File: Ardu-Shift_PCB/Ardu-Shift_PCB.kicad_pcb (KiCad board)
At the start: 2 copper layers, 103.5 x 62.2 mm, 16 parts, among them U1 OLED(SPI), U2 Arduino_Pro_Micro

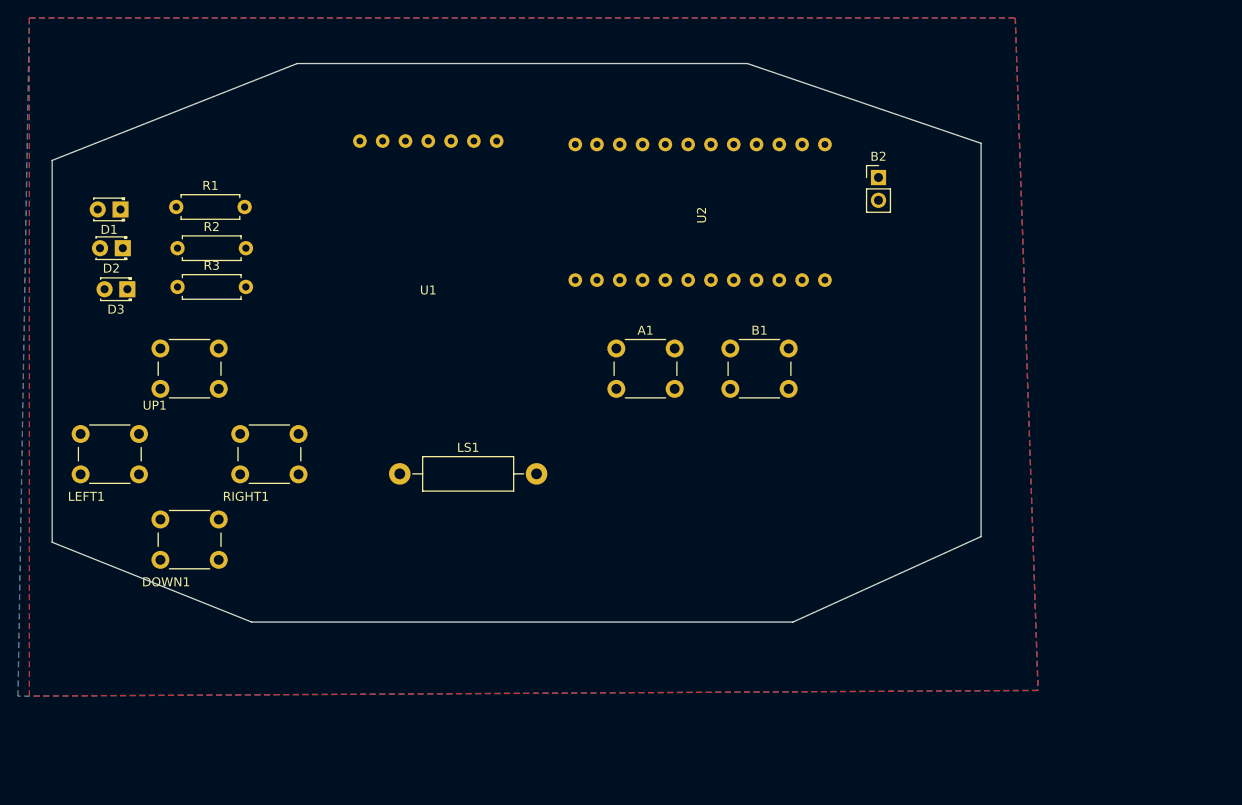
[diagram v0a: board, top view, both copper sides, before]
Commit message: more 'realistic' adjustments to the location of electronics on the PCB
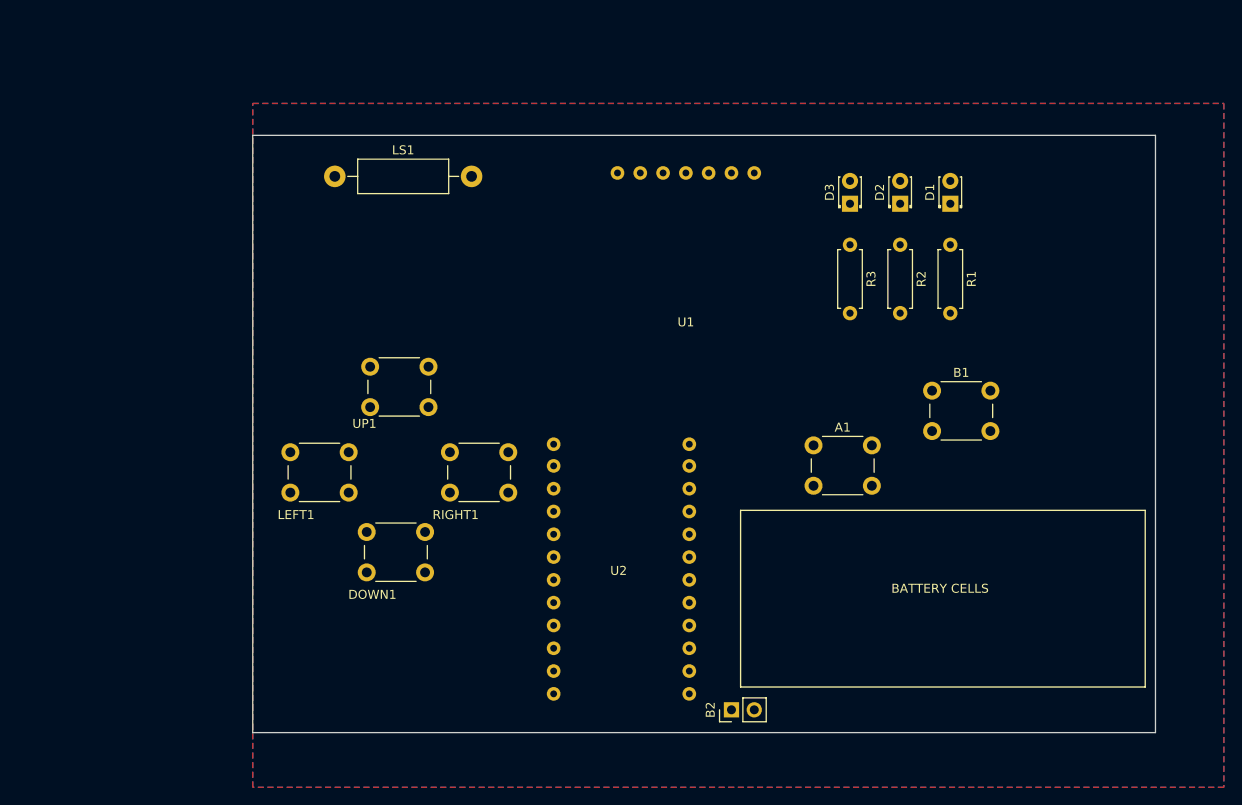
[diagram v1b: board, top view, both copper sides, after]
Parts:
- moved D1 92.5 mm to (115.3, 41.7), turned to 90 degrees
- moved D2 86.8 mm to (109.7, 41.7), turned to 90 degrees
- moved R1 86.4 mm to (115.3, 46.2), turned to 270 degrees
- moved D3 81.1 mm to (104.1, 41.7), turned to 90 degrees
- moved R2 80.5 mm to (109.7, 46.2), turned to 270 degrees
- moved R3 75.1 mm to (104.1, 46.2), turned to 270 degrees
- moved B2 61.5 mm to (90.9, 98.0), turned to 90 degrees
- moved U2 45.6 mm to (78.7, 86.4), turned to 180 degrees
- moved LS1 33.9 mm to (46.7, 38.6)
- moved U1 28.9 mm to (85.9, 54.4)
- moved A1 24.5 mm to (100.1, 68.6)
- moved LEFT1 23.5 mm to (41.8, 69.3)
- moved RIGHT1 23.5 mm to (59.6, 69.3)
- moved UP1 23.5 mm to (50.7, 59.8)
- moved DOWN1 23.0 mm to (50.3, 78.2)
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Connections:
- DOWN1 pad 2: Net-(DOWN1-Pad2) -> BAT-
- LEFT1 pad 1: Net-(LEFT1-Pad1) -> LEFT
- LEFT1 pad 2: BAT- -> Net-(LEFT1-Pad2)
- RIGHT1 pad 2: BAT- -> Net-(RIGHT1-Pad2)
- U2 pad 2: UP -> B
- U2 pad 3: LEFT -> A
- U2 pad 4: RIGHT -> Speaker-
- U2 pad 5: DOWN -> Speaker+
- U2 pad A0: B -> UP
- U2 pad A1: A -> LEFT
- U2 pad A2: Speaker- -> RIGHT
- U2 pad A3: Speaker+ -> DOWN
- UP1 pad 1: UP -> Net-(UP1-Pad1)
- UP1 pad 2: BAT- -> Net-(UP1-Pad2)
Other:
- board size 103.5 x 62.2 mm -> 100.6 x 66.5 mm

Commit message: first version of the final assembly/routing of game-device PCB
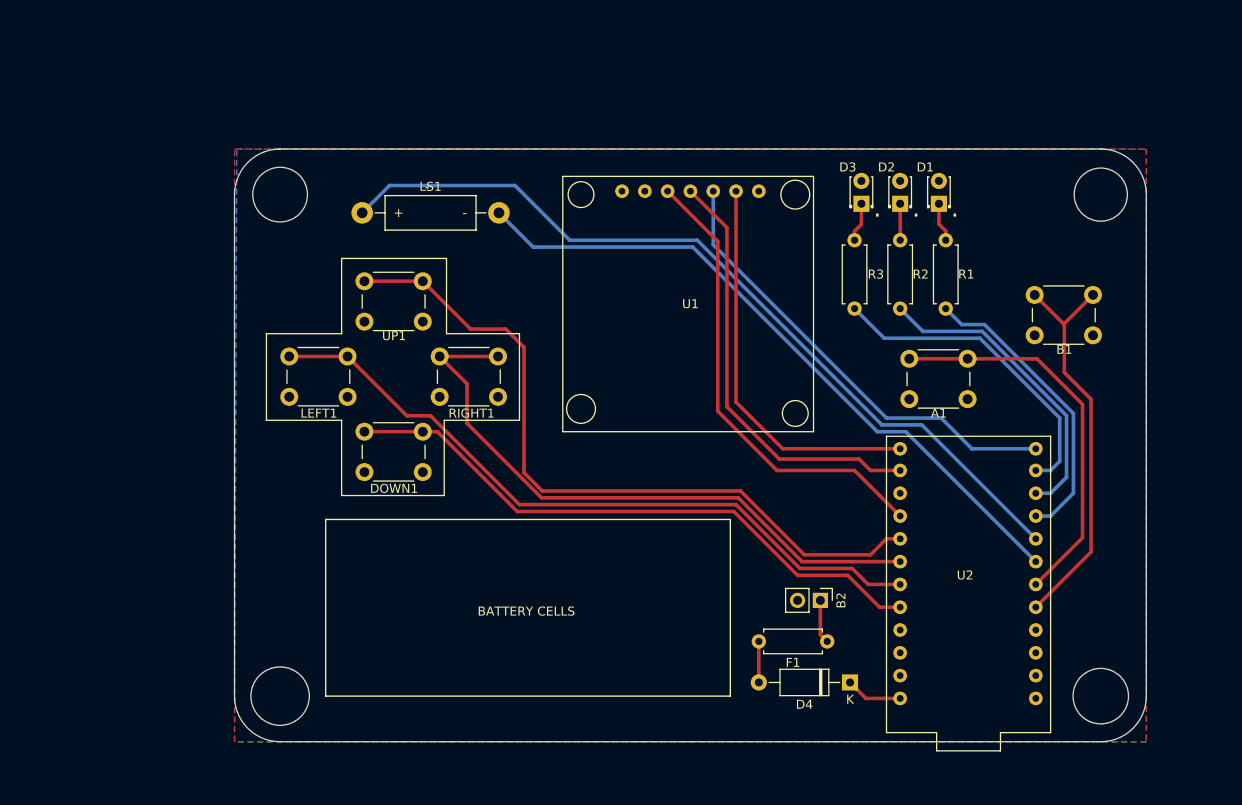
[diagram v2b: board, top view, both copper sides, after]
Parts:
- added D4: D, Diode_THT:D_A-405_P10.16mm_Horizontal, F.Cu at (104.1, 95.0)
- added F1: Polyfuse500mA, Resistor_THT:R_Axial_DIN0207_L6.3mm_D2.5mm_P7.62mm_Horizontal, F.Cu at (101.6, 90.4)
- moved U2 38.6 mm to (117.3, 86.9)
- moved B2 15.7 mm to (100.8, 85.9), turned to 270 degrees
- moved B1 15.6 mm to (124.7, 51.8)
- moved A1 14.4 mm to (110.7, 58.9)
- moved DOWN1 11.2 mm to (50.0, 67.1)
- moved RIGHT1 10.7 mm to (58.4, 58.7)
- moved LEFT1 10.7 mm to (41.7, 58.7)
- moved UP1 9.55 mm to (50.0, 50.3)
- moved LS1 5.08 mm to (49.8, 42.7)
- moved U1 2.09 mm to (86.4, 56.4)
- moved D1 1.27 mm to (114.0, 41.7)
- moved D3 1.27 mm to (105.4, 41.7)
- moved R1 0.72 mm to (114.8, 45.7)
- moved R3 0.72 mm to (104.6, 45.7)
- moved R2 0.51 mm to (109.7, 45.7)
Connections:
- net A renamed A_Button
- net B renamed B_Button
- net RESET renamed Net-(U2-PadRST)
- A1 pad 2: BAT- -> GND
- B1 pad 2: BAT- -> GND
- B2 pad 1: BAT+ -> Net-(B2-Pad1)
- B2 pad 2: BAT- -> GND
- DOWN1 pad 2: BAT- -> GND
- LEFT1 pad 2: Net-(LEFT1-Pad2) -> GND
- R1 pad 2: R_LED -> B_LED
- R3 pad 2: B_LED -> R_LED
- RIGHT1 pad 1: Net-(RIGHT1-Pad1) -> RIGHT
- RIGHT1 pad 2: Net-(RIGHT1-Pad2) -> GND
- U1 pad CS: BAT- -> GND
- U1 pad GND: BAT- -> GND
- U2 pad A1: LEFT -> RIGHT
- U2 pad A2: RIGHT -> LEFT
- U2 pad GND: BAT- -> GND
- UP1 pad 1: Net-(UP1-Pad1) -> UP
- UP1 pad 2: Net-(UP1-Pad2) -> GND
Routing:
- net Speaker+: track 0.00 -> 92.6 mm
- net UP: track 0.00 -> 81.2 mm
- net LEFT: track 0.00 -> 78.6 mm
- net Speaker-: track 0.00 -> 75.9 mm
- net RIGHT: track 0.00 -> 69.9 mm
- net DOWN: track 0.00 -> 67.8 mm
- net SCK: track 0.00 -> 52.0 mm
- net RES: track 0.00 -> 51.3 mm
- net MOSI: track 0.00 -> 47.9 mm
- net B_Button: track 0.00 -> 44.6 mm
- net CE: track 0.00 -> 43.9 mm
- net A_Button: track 0.00 -> 43.6 mm
- net R_LED: track 0.00 -> 35.8 mm
- net G_LED: track 0.00 -> 34.5 mm
- net B_LED: track 0.00 -> 33.2 mm
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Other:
- board size 100.6 x 66.5 mm -> 101.6 x 66 mm
- board text added: "+"
- board text added: "-"
- board text added: "."

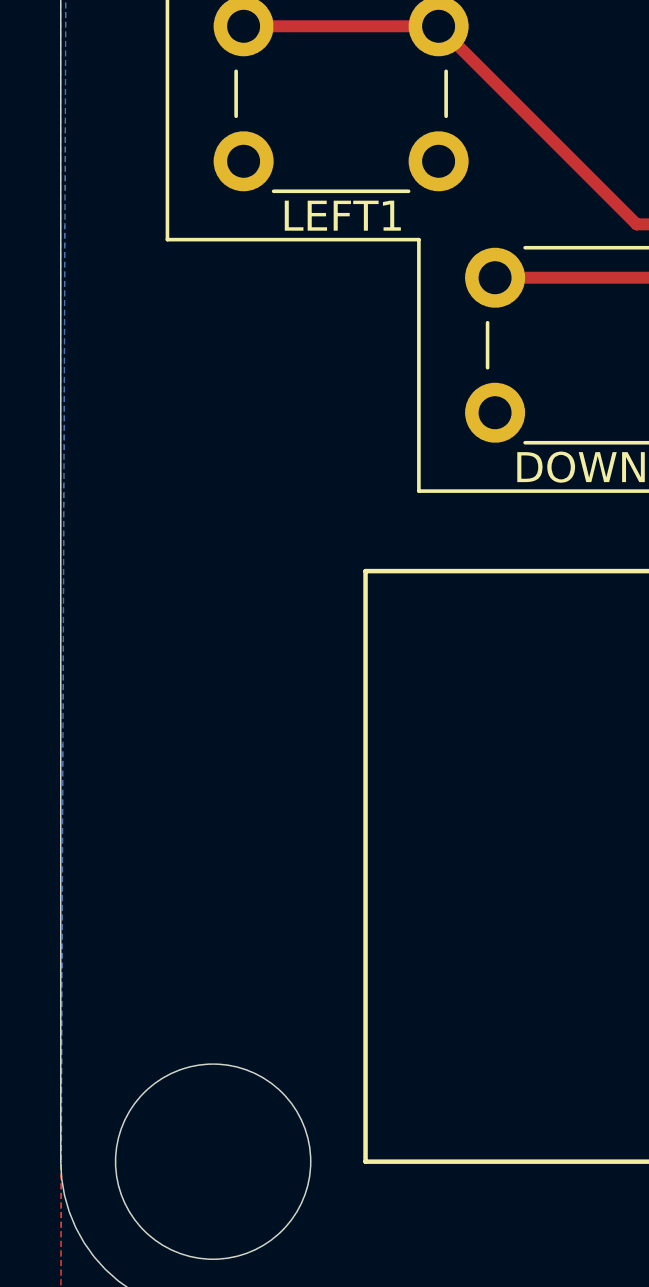
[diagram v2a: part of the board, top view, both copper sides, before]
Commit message: added Ardu-shift branding to PCB on both silk layers
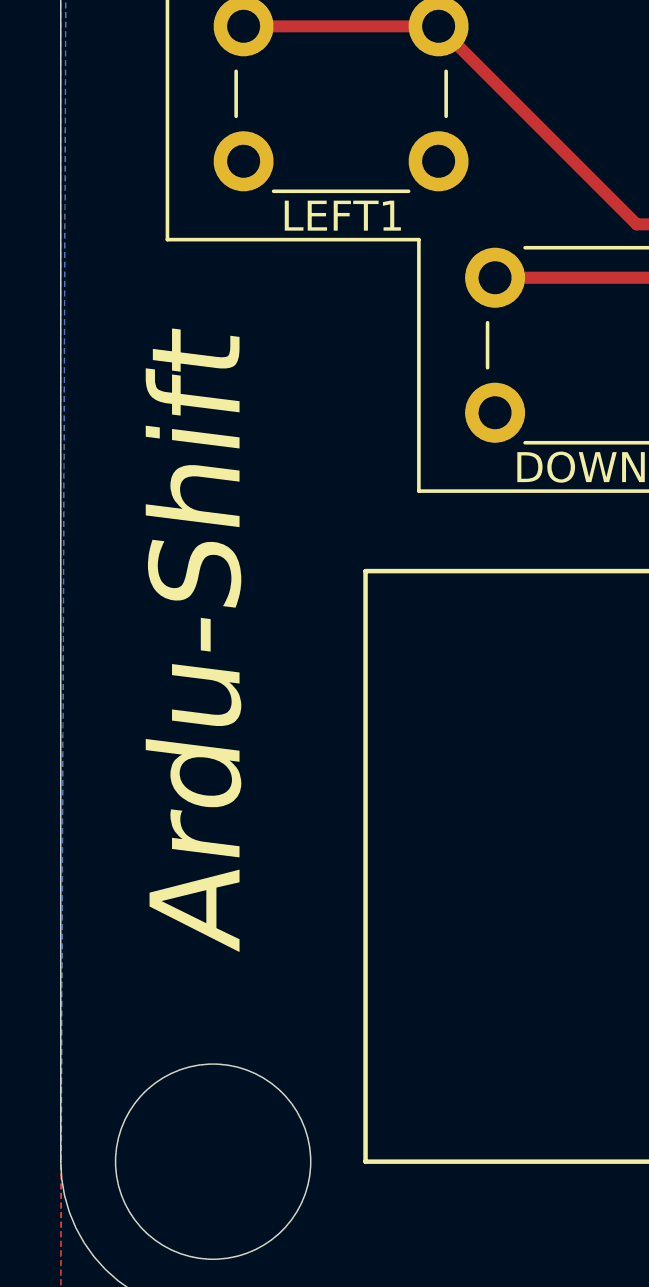
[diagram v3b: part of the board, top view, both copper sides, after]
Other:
- board text added: "Ardu-Shift"
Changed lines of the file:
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@@
   (general
     (thickness 1.6)
-    (drawings 54)
+    (drawings 56)
     (tracks 111)
     (zones 0)
@@
       (padsonsilk false)
       (subtractmaskfromsilk false)
-      (outputformat 1)
+      (outputformat 4)
       (mirror false)
-      (drillshape 1)
+      (drillshape 0)
       (scaleselection 1)
       (outputdirectory ""))
@@
     )
   )
+  (gr_text Ardu-Shift (at 40.386 80.01 90) (layer B.SilkS)
+    (effects (font (size 3 3) (thickness 0.3) italic) (justify mirror))
+  )
+  (gr_text Ardu-Shift (at 40.132 79.248 90) (layer F.SilkS)
+    (effects (font (size 3 3) (thickness 0.3) italic))
+  )
   (gr_line (start 126.492 67.564) (end 126.492 100.584) (layer F.SilkS) (width 0.12))

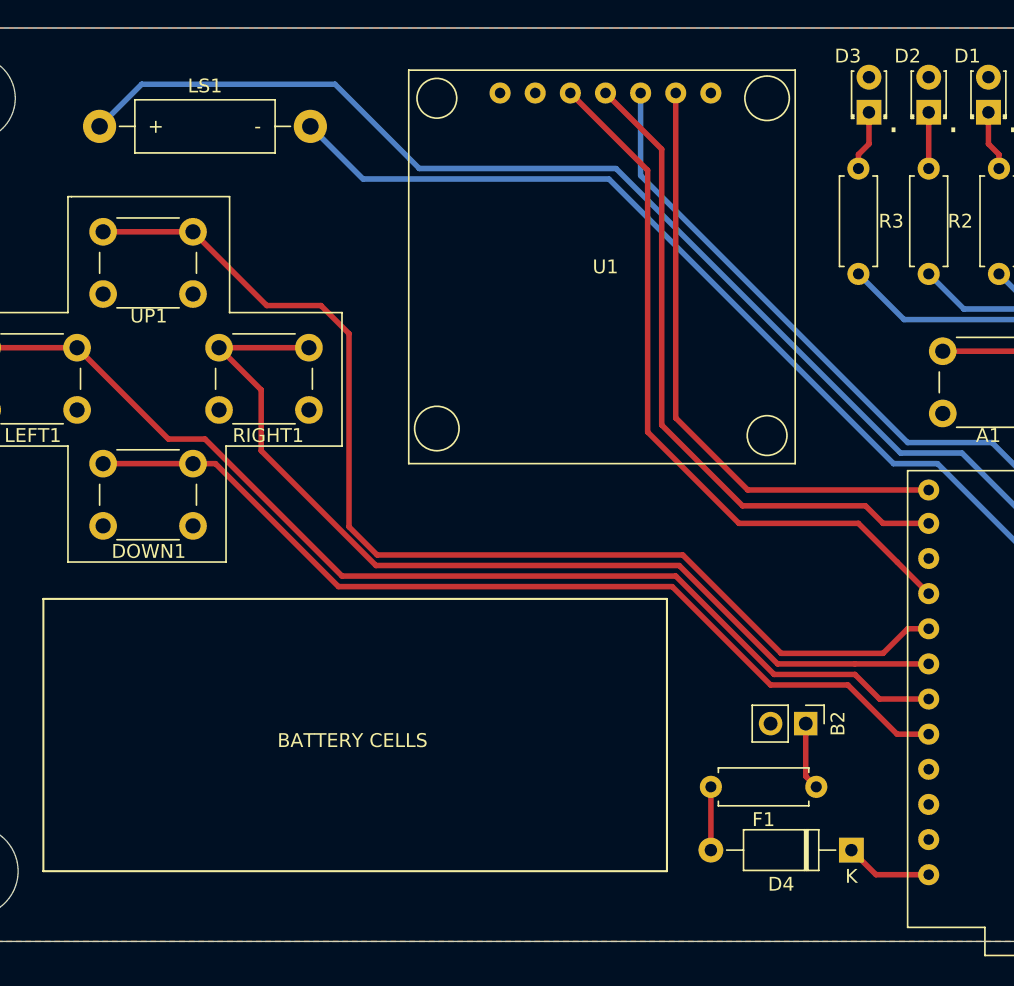
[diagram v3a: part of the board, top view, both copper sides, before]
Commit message: added a power switch to ground for on/off functionality, added footprint for smaller speaker and updated all files.PDFs
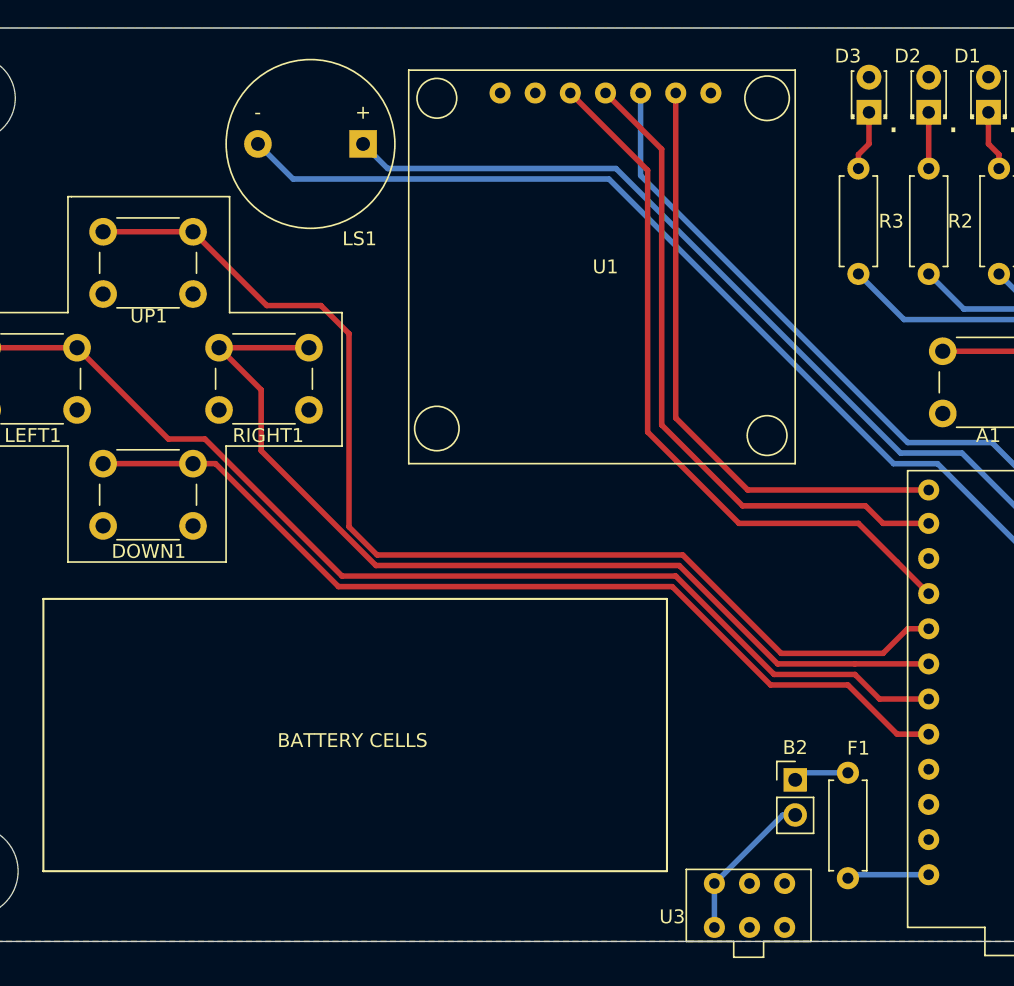
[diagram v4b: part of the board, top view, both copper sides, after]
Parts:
- removed D4: D, Diode_THT:D_A-405_P10.16mm_Horizontal
- added U3: SPDT_Slide, Button_Switch_THT:SPDT_Slide, F.Cu at (96.8, 99.1)
- LS1: footprint Resistor_THT:R_Axial_DIN0411_L9.9mm_D3.6mm_P15.24mm_Horizontal -> Buzzer_Beeper:Buzzer_12x9.5RM7.6
- moved LS1 19.1 mm to (68.8, 43.9), turned to 180 degrees
- moved B2 4.13 mm to (100.1, 89.9), turned to 0 degrees
- moved F1 2.50 mm to (103.9, 89.4), turned to 270 degrees
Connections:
- B2 pad 2: GND -> Net-(B2-Pad2)
- F1 pad 2: Net-(D4-Pad2) -> BAT+
- LEFT1 pad 1: LEFT -> Net-(LEFT1-Pad1)
- LEFT1 pad 2: GND -> Net-(LEFT1-Pad2)
- RIGHT1 pad 1: RIGHT -> Net-(RIGHT1-Pad1)
- RIGHT1 pad 2: GND -> Net-(RIGHT1-Pad2)
- UP1 pad 2: GND -> Net-(UP1-Pad2)
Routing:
- net Speaker+: track 92.6 -> 70.5 mm
- net Net-(B2-Pad2): track 0.00 -> 11.1 mm
- net Net-(D4-Pad2): track 4.57 -> 0.00 mm
- net Speaker-: track 75.9 -> 79.2 mm
- net Net-(B2-Pad1): track 4.89 -> 4.02 mm
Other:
- board text removed: "+"
